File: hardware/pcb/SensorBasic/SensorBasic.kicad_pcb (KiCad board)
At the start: 2 copper layers, 29 parts, among them U1 MicroC_Header, U2 DS7505, U3 74HC595-PWR

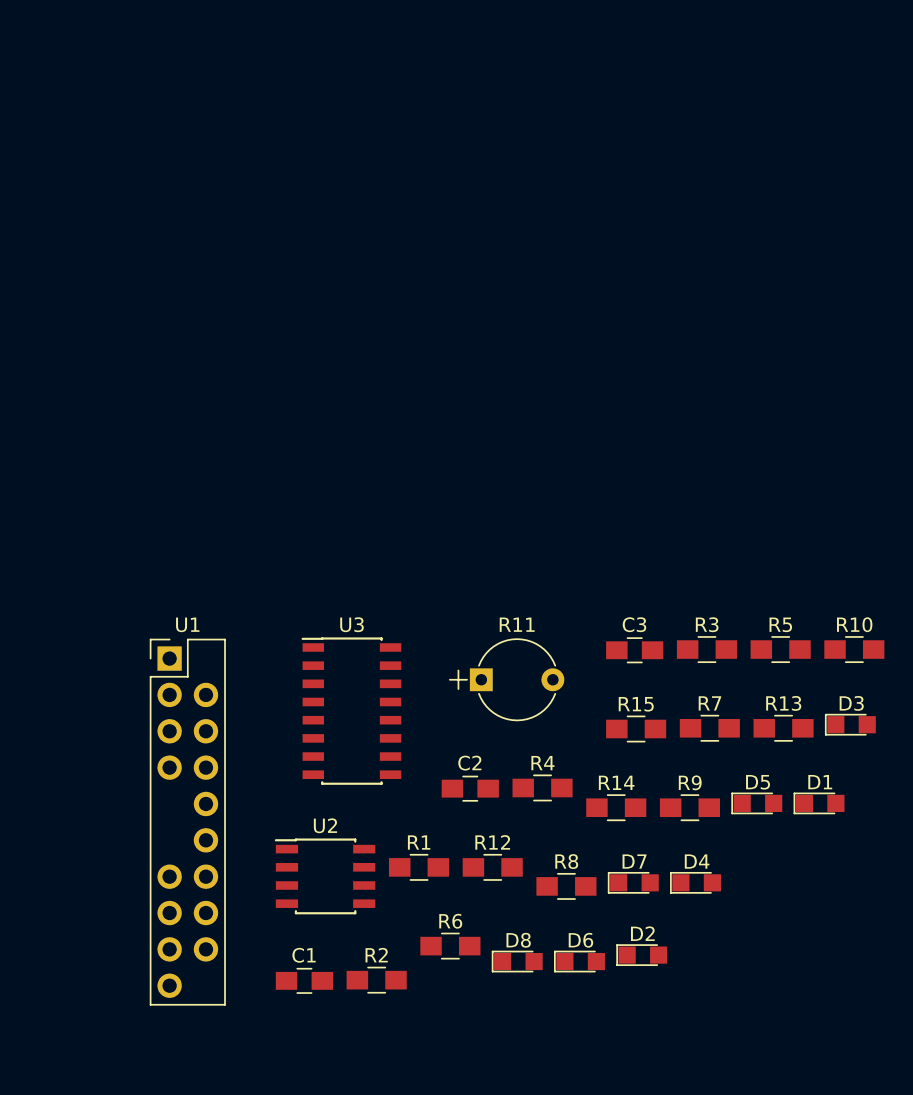
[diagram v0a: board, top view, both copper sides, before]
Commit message: First layout with initial placements of ICs and LEDs. Still need to place the resistors, capacitors, and route traces
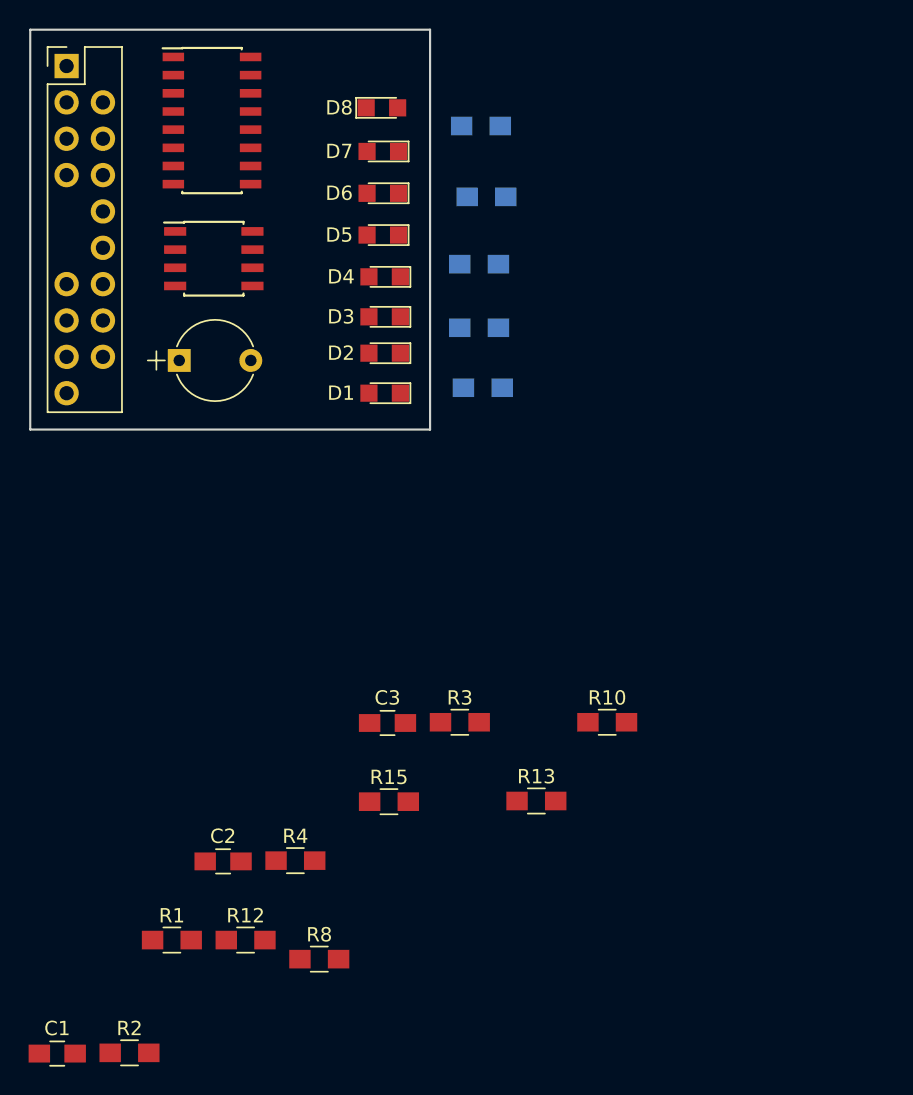
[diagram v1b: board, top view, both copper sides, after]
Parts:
- R14, R5, R6, R7, R9: moved to B.Cu
- moved D8 60.4 mm to (131.3, 43.6)
- moved D6 55.4 mm to (131.3, 49.5), turned to 180 degrees
- moved D7 54.0 mm to (131.3, 46.6), turned to 180 degrees
- moved R9 49.8 mm to (138.2, 44.8)
- moved D4 47.6 mm to (131.4, 55.4), turned to 180 degrees
- moved D5 47.6 mm to (131.3, 52.5), turned to 180 degrees
- moved D2 45.8 mm to (131.4, 60.7), turned to 180 degrees
- moved U2 43.9 mm to (119.5, 54.1)
- moved R14 43.6 mm to (138.6, 49.8)
- moved D3 43.3 mm to (131.4, 58.2), turned to 180 degrees
- moved R6 43.3 mm to (138.0, 58.9)
- moved U3 42.4 mm to (119.4, 44.5)
- moved U1 42.0 mm to (109.2, 40.6)
- moved D1 41.8 mm to (131.4, 63.5), turned to 180 degrees
- moved R7 36.2 mm to (138.0, 54.5)
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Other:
- board outline added: 27.9 x 27.9 mm

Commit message: First iteration of adding traces
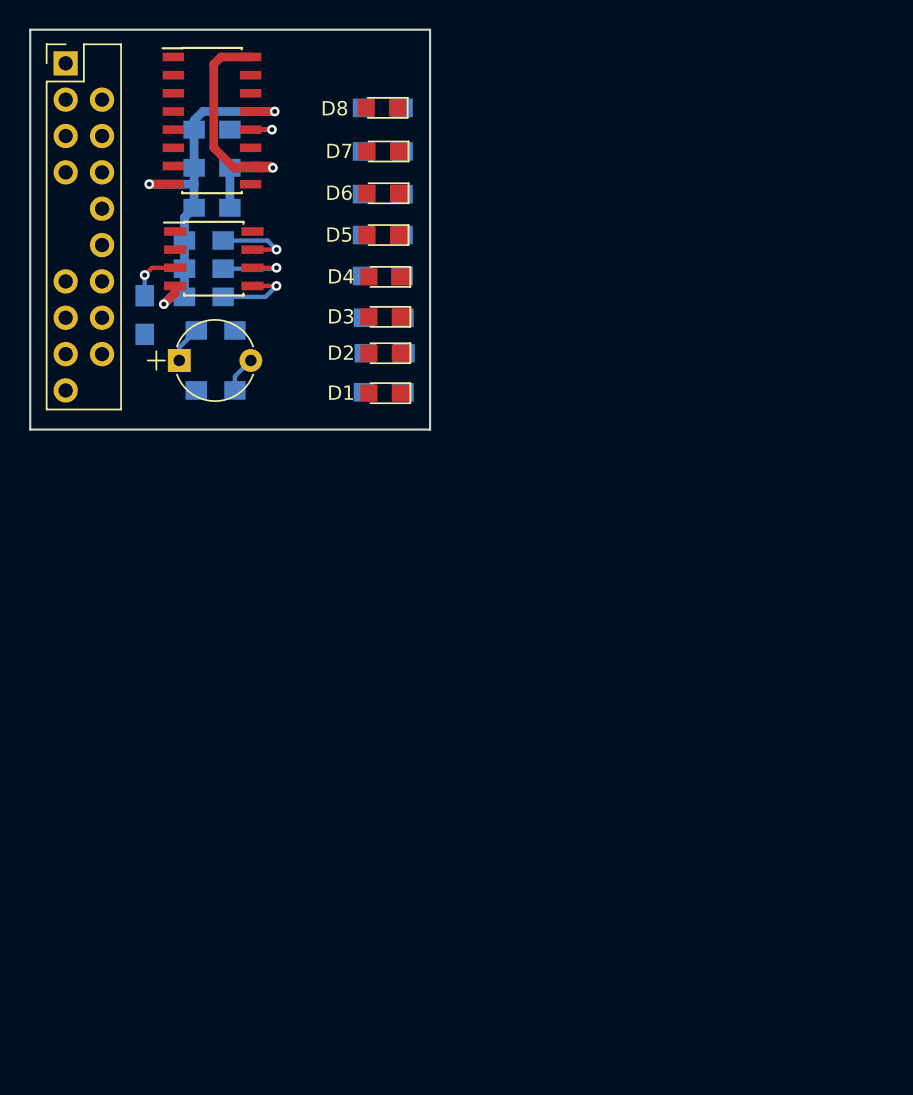
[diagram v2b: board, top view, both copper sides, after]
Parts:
- C1, C2, C3, R1, R10, R12, R13, R15, R2, R3, R4, R8: moved to B.Cu
- moved C1 65.5 mm to (119.4, 45.1), turned to 180 degrees
- moved R2 53.1 mm to (118.8, 56.8), turned to 180 degrees
- moved R15 48.5 mm to (131.3, 43.6), turned to 180 degrees
- moved R8 47.9 mm to (131.3, 55.3)
- moved C2 45.7 mm to (119.4, 50.5)
- moved R4 43.8 mm to (118.8, 52.8), turned to 180 degrees
- moved R13 43.7 mm to (131.3, 49.6)
- moved R1 43.7 mm to (114.7, 58.0), turned to 90 degrees
- moved C3 40.7 mm to (119.4, 47.8)
- moved R10 38.7 mm to (119.6, 59.1), turned to 180 degrees
- moved R12 38.5 mm to (119.6, 63.3), turned to 180 degrees
- moved R3 36.4 mm to (118.8, 54.8), turned to 180 degrees
- moved R9 10.3 mm to (131.3, 52.5)
- moved R14 7.90 mm to (131.3, 46.6), turned to 180 degrees
- moved R7 7.65 mm to (131.4, 58.2)
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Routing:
- net GND: track 0.00 -> 28.5 mm, vias 0 -> 3
- net /3.3V: track 0.00 -> 20.7 mm, vias 0 -> 1
- net Net-(R2-Pad1): track 0.00 -> 5.73 mm, vias 0 -> 1
- net Net-(R4-Pad1): track 0.00 -> 5.67 mm, vias 0 -> 1
- net Net-(R3-Pad1): track 0.00 -> 5.44 mm, vias 0 -> 1
- net /latchPin: track 0.00 -> 4.43 mm, vias 0 -> 1
- net /OS: track 0.00 -> 3.78 mm, vias 0 -> 1
- net /PR_TOP: track 0.00 -> 2.59 mm
- net /PR_BOT: track 0.00 -> 2.56 mm
- net Net-(D6-Pad2): track 0.00 -> 0.54 mm
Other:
- net class Default: clearance 0.2 -> 0.1524; trace_width 0.25 -> 0.1524; via_dia 0.6 -> 0.6858; via_drill 0.4 -> 0.3302
- rule trace_clearance: 0.2 -> 0.1524
- rule trace_min: 0.2 -> 0.1524
- rule via_min_drill: 0.3 -> 0.3302
- rule via_min_size: 0.4 -> 0.6858

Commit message: First version of final layout
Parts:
- moved R1 4.55 mm to (114.0, 53.5), turned to 270 degrees
- moved C1 4.06 mm to (123.4, 45.1), turned to 0 degrees
- moved C3 4.06 mm to (123.4, 47.7), turned to 180 degrees
- moved C2 1.94 mm to (119.0, 48.6)
- moved R6 0.83 mm to (130.7, 60.4), turned to 180 degrees
- moved R5 0.80 mm to (130.6, 63.2), turned to 180 degrees
- moved D5 0.77 mm to (130.6, 52.1)
- moved D6 0.77 mm to (130.6, 49.2)
- moved D7 0.77 mm to (130.6, 46.3)
- moved R14 0.77 mm to (130.6, 46.3)
- moved R15 0.77 mm to (130.6, 43.2)
- moved R9 0.77 mm to (130.6, 52.1), turned to 180 degrees
- moved R13 0.77 mm to (130.6, 49.3), turned to 180 degrees
- moved D1 0.77 mm to (130.7, 63.2)
- moved D2 0.77 mm to (130.7, 60.4)
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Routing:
- net /5V: track 0.00 -> 64.6 mm
- net GND: track 28.5 -> 72.2 mm, vias 3 -> 4
- net Net-(D2-Pad2): track 0.00 -> 29.4 mm, vias 0 -> 2
- net Net-(D3-Pad2): track 0.00 -> 28.9 mm, vias 0 -> 2
- net Net-(D4-Pad2): track 0.00 -> 28.4 mm
- net Net-(D1-Pad2): track 0.00 -> 26.7 mm, vias 0 -> 2
- net /OS: track 3.78 -> 29.5 mm
- net Net-(D5-Pad2): track 0.00 -> 21.8 mm, vias 0 -> 2
- net /clockPin: track 0.00 -> 20.3 mm, vias 0 -> 1
- net Net-(D6-Pad2): track 0.54 -> 20.7 mm, vias 0 -> 2
- net Net-(D7-Pad2): track 0.41 -> 18.1 mm, vias 0 -> 2
- net /PR_BOT: track 2.56 -> 14.2 mm
- net /latchPin: track 4.43 -> 16.1 mm
- net /dataPin: track 0.00 -> 11.6 mm, vias 0 -> 1
- net /PR_TOP: track 2.59 -> 11.8 mm
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
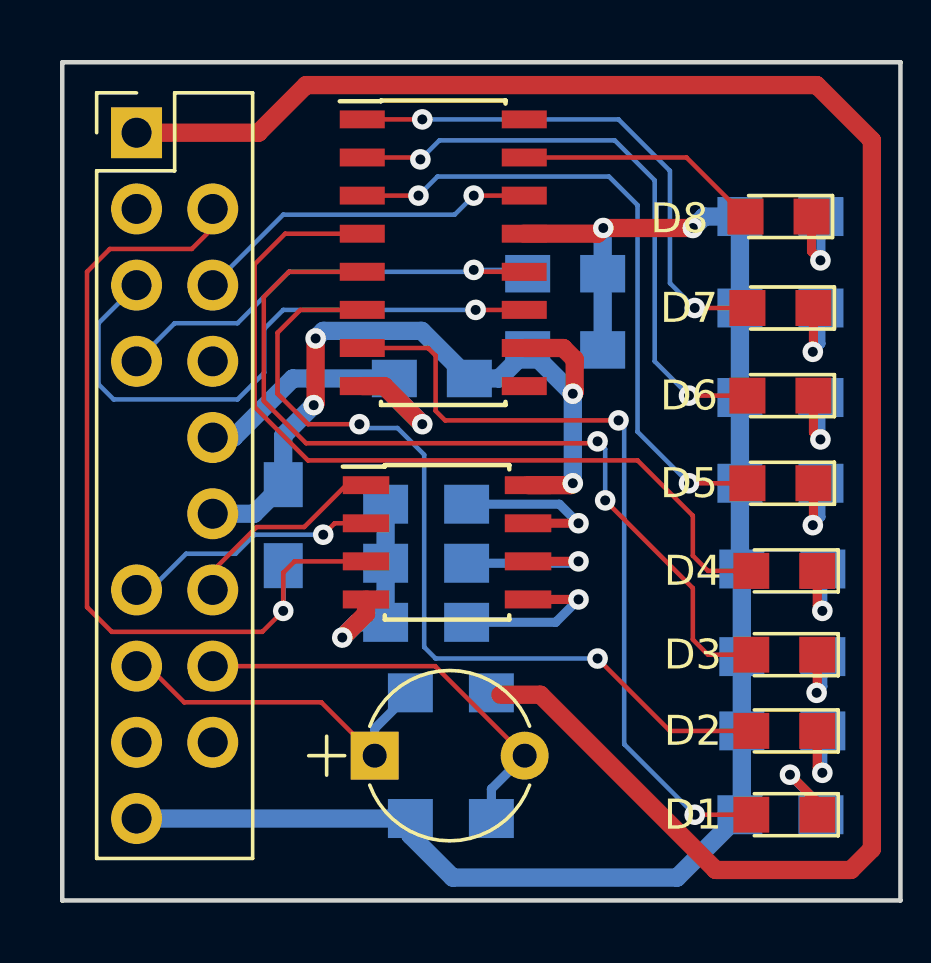
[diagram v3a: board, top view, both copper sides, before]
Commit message: Added MPN part numbers to all parts except the resistors
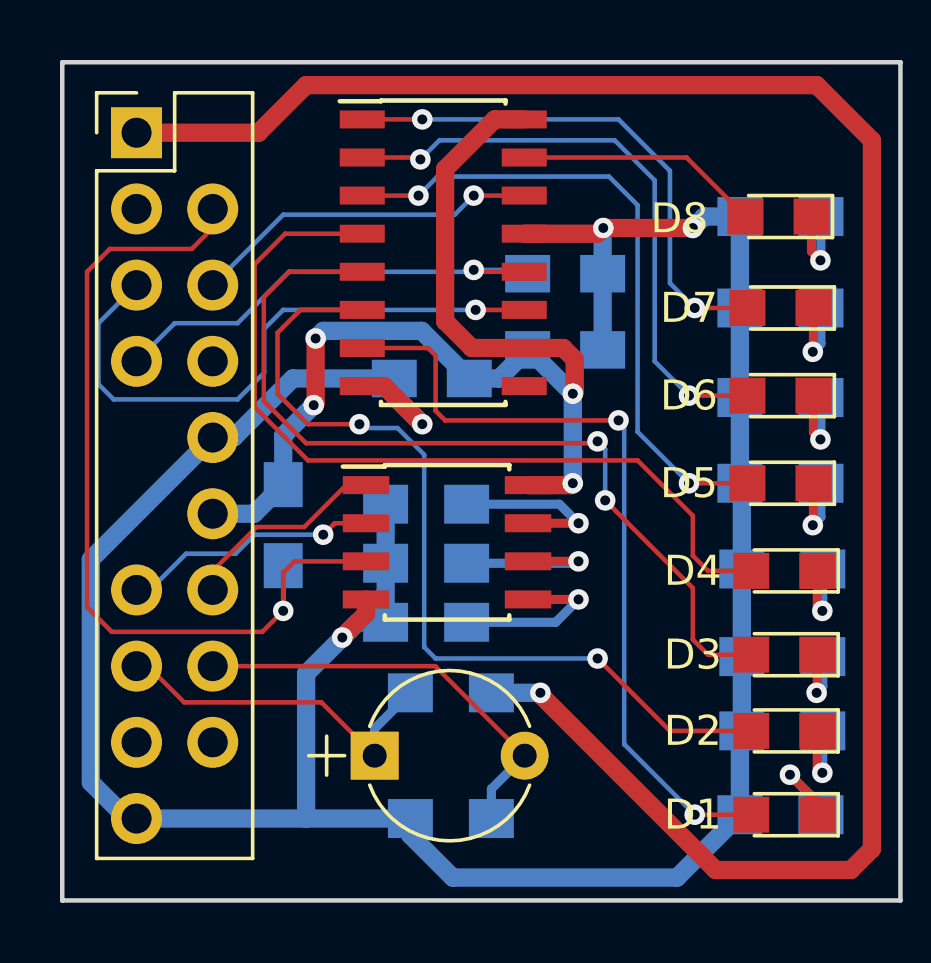
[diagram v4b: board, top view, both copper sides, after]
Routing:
- net GND: track 72.2 -> 94.1 mm
- net /3.3V: track 25.9 -> 37.3 mm
- net /5V: track 64.6 -> 65.0 mm, vias 0 -> 1
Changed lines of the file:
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@@
   (general
     (links 57)
-    (no_connects 6)
-    (area 104.797909 37.1921 136.796281 66.6669)
+    (no_connects 0)
+    (area 104.797909 37.1921 134.695001 66.6669)
     (thickness 1.6)
     (drawings 4)
-    (tracks 266)
+    (tracks 284)
     (zones 0)
     (modules 29)
@@
     (pad_to_mask_clearance 0.2)
     (aux_axis_origin 0 0)
-    (visible_elements FFFFF77F)
+    (visible_elements FFFFFF7F)
     (pcbplotparams
       (layerselection 0x00030_80000001)
@@
   (via (at 120.396 45.0215) (size 0.6858) (drill 0.3302) (layers F.Cu B.Cu) (net 1))
   (segment (start 120.4595 45.085) (end 120.396 45.0215) (width 0.1524) (layer F.Cu) (net 1))
+  (segment (start 129.333 57.912) (end 129.333 60.3885) (width 0.6096) (layer B.Cu) (net 2) (status C00000))
+  (segment (start 129.333 60.3885) (end 129.2695 60.452) (width 0.6096) (layer B.Cu) (net 2) (status C00000))
+  (segment (start 129.2695 60.452) (end 129.2695 63.1825) (width 0.6096) (layer B.Cu) (net 2) (status C00000))
+  (segment (start 129.333 54.991) (end 129.333 52.197) (width 0.6096) (layer B.Cu) (net 2) (status C00000))
+  (segment (start 129.333 52.197) (end 129.2695 52.1335) (width 0.6096) (layer B.Cu) (net 2) (status C00000))
+  (segment (start 129.2695 52.1335) (end 129.2695 49.276) (width 0.6096) (layer B.Cu) (net 2) (status C00000))
+  (segment (start 109.1565 63.3095) (end 108.839 63.3095) (width 0.6096) (layer B.Cu) (net 2) (status C00000))
+  (segment (start 108.839 63.3095) (end 107.6325 62.103) (width 0.6096) (layer B.Cu) (net 2) (status 400000))
+  (segment (start 107.6325 54.6735) (end 111.6965 50.6095) (width 0.6096) (layer B.Cu) (net 2) (status 800000))
+  (segment (start 107.6325 62.103) (end 107.6325 54.6735) (width 0.6096) (layer B.Cu) (net 2))
+  (segment (start 114.808 63.3095) (end 114.808 58.4835) (width 0.6096) (layer B.Cu) (net 2))
+  (segment (start 114.808 58.4835) (end 116.0145 57.277) (width 0.6096) (layer B.Cu) (net 2))
   (segment (start 117.749 48.641) (end 117.749 49.2325) (width 0.6096) (layer B.Cu) (net 2))
   (segment (start 117.749 49.2325) (end 118.6815 50.165) (width 0.6096) (layer B.Cu) (net 2))
@@
   (segment (start 127.174 65.278) (end 129.333 63.119) (width 0.6096) (layer B.Cu) (net 2))
   (segment (start 119.6975 65.278) (end 127.174 65.278) (width 0.6096) (layer B.Cu) (net 2))
-  (segment (start 129.333 63.119) (end 129.333 57.912) (width 0.6096) (layer B.Cu) (net 2))
   (segment (start 129.333 57.912) (end 129.333 54.991) (width 0.6096) (layer B.Cu) (net 2))
   (segment (start 129.333 54.991) (end 129.2695 54.9275) (width 0.6096) (layer B.Cu) (net 2))
-  (segment (start 129.2695 54.9275) (end 129.2695 49.276) (width 0.6096) (layer B.Cu) (net 2))
   (segment (start 129.2695 49.276) (end 129.2695 46.2915) (width 0.6096) (layer B.Cu) (net 2))
   (segment (start 129.2695 46.2915) (end 129.2695 43.2435) (width 0.6096) (layer B.Cu) (net 2))
-  (segment (start 109.1565 63.3095) (end 118.284 63.3095) (width 0.6096) (layer B.Cu) (net 2))
+  (segment (start 109.1565 63.3095) (end 114.808 63.3095) (width 0.6096) (layer B.Cu) (net 2))
+  (segment (start 114.808 63.3095) (end 118.284 63.3095) (width 0.6096) (layer B.Cu) (net 2))
   (segment (start 129.333 54.991) (end 129.2695 54.9275) (width 0.6096) (layer B.Cu) (net 2))
   (segment (start 117.4585 54.8005) (end 117.4585 52.832) (width 0.6096) (layer B.Cu) (net 2))
   (segment (start 117.4585 56.769) (end 117.4585 54.8005) (width 0.6096) (layer B.Cu) (net 2))
   (segment (start 116.807 56.007) (end 116.807 56.4845) (width 0.6096) (layer F.Cu) (net 2))
+  (segment (start 116.807 56.4845) (end 116.0145 57.277) (width 0.6096) (layer F.Cu) (net 2))
+  (via (at 116.0145 57.277) (size 0.6858) (drill 0.3302) (layers F.Cu B.Cu) (net 2))
   (segment (start 116.5225 56.769) (end 117.4585 56.769) (width 0.6096) (layer B.Cu) (net 2))
   (segment (start 116.0145 57.277) (end 116.5225 56.769) (width 0.6096) (layer B.Cu) (net 2))
-  (via (at 116.0145 57.277) (size 0.6858) (drill 0.3302) (layers F.Cu B.Cu) (net 2))
-  (segment (start 116.807 56.4845) (end 116.0145 57.277) (width 0.6096) (layer F.Cu) (net 2))
+  (segment (start 122.08 40.005) (end 121.0945 40.005) (width 0.6096) (layer F.Cu) (net 3) (status 400000))
+  (segment (start 120.3325 47.625) (end 122.08 47.625) (width 0.6096) (layer F.Cu) (net 3) (status 800000))
+  (segment (start 119.4435 46.736) (end 120.3325 47.625) (width 0.6096) (layer F.Cu) (net 3))
+  (segment (start 119.4435 41.656) (end 119.4435 46.736) (width 0.6096) (layer F.Cu) (net 3))
+  (segment (start 121.0945 40.005) (end 119.4435 41.656) (width 0.6096) (layer F.Cu) (net 3))
   (segment (start 114.046 52.1805) (end 114.046 50.546) (width 0.6096) (layer B.Cu) (net 3))
   (segment (start 118.6615 47.0535) (end 120.249 48.641) (width 0.6096) (layer B.Cu) (net 3))
@@
   (segment (start 123.8885 53.467) (end 123.2535 52.832) (width 0.3048) (layer B.Cu) (net 23))
   (via (at 123.8885 53.467) (size 0.6858) (drill 0.3302) (layers F.Cu B.Cu) (net 23))
-  (segment (start 109.1565 40.4495) (end 113.2205 40.4495) (width 0.6096) (layer F.Cu) (net 24))
-  (segment (start 122.6185 59.182) (end 121.285 59.182) (width 0.6096) (layer F.Cu) (net 24))
+  (segment (start 120.984 59.1185) (end 122.6185 59.1185) (width 0.6096) (layer B.Cu) (net 24) (status 400000))
+  (segment (start 113.2205 40.4495) (end 114.808 38.862) (width 0.6096) (layer F.Cu) (net 24))
+  (segment (start 114.808 38.862) (end 131.826 38.862) (width 0.6096) (layer F.Cu) (net 24))
+  (segment (start 131.826 38.862) (end 133.6675 40.7035) (width 0.6096) (layer F.Cu) (net 24))
+  (segment (start 133.6675 40.7035) (end 133.6675 64.3255) (width 0.6096) (layer F.Cu) (net 24))
+  (segment (start 133.6675 64.3255) (end 132.969 65.024) (width 0.6096) (layer F.Cu) (net 24))
+  (segment (start 132.969 65.024) (end 128.4605 65.024) (width 0.6096) (layer F.Cu) (net 24))
   (segment (start 128.4605 65.024) (end 122.6185 59.182) (width 0.6096) (layer F.Cu) (net 24))
-  (segment (start 132.969 65.024) (end 128.4605 65.024) (width 0.6096) (layer F.Cu) (net 24))
-  (segment (start 133.6675 64.3255) (end 132.969 65.024) (width 0.6096) (layer F.Cu) (net 24))
-  (segment (start 133.6675 40.7035) (end 133.6675 64.3255) (width 0.6096) (layer F.Cu) (net 24))
-  (segment (start 131.826 38.862) (end 133.6675 40.7035) (width 0.6096) (layer F.Cu) (net 24))
-  (segment (start 114.808 38.862) (end 131.826 38.862) (width 0.6096) (layer F.Cu) (net 24))
-  (segment (start 113.2205 40.4495) (end 114.808 38.862) (width 0.6096) (layer F.Cu) (net 24))
+  (segment (start 113.2205 40.4495) (end 109.1565 40.4495) (width 0.6096) (layer F.Cu) (net 24))
+  (segment (start 122.6185 59.1185) (end 122.6185 59.182) (width 0.6096) (layer F.Cu) (net 24))
+  (via (at 122.6185 59.1185) (size 0.6858) (drill 0.3302) (layers F.Cu B.Cu) (net 24))
   (segment (start 109.1565 58.2295) (end 109.5375 58.2295) (width 0.1524) (layer F.Cu) (net 25))
   (segment (start 109.5375 58.2295) (end 110.744 59.436) (width 0.1524) (layer F.Cu) (net 25))
